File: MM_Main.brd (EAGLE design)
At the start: 72 x 92 mm, 76 parts, among them IC1 ULN2003AD, IC2 TB6612FNG, IC4 LD117ADT50TR, Q1 TEFT4300, Q2 TEFT4300, Q3 TEFT4300, Q4 TEFT4300, Q5 TEFT4300, Q6 TEFT4300, Q7 8MHz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

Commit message: wszystkie sciezki polaczone \!
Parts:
- removed C_V3: 100n, rcl:C0805
- removed R14, R15: 47k, resistor:R0805
- removed SG2: F/QMX, buzzer:F/QMX
- added BAT1, BOOT: (no value), pinhead:1X03
- added BUZ1: BUZZER-9.5MM-3V?, _microMouse:BUZZER-9.5MM
- added S2: (no value), adafruit:EG1218
- moved C21 80.5 mm to (18.4, -20.8), flipped to the bottom
- moved C22 71.9 mm to (11.7, -40.8), flipped to the bottom, turned to 90 degrees
- moved C_V2 70.0 mm to (7.14, 11.3)
- moved C_V1 63.1 mm to (7.94, -8.26), flipped to the bottom
- moved C15 56.8 mm to (11.6, -46.5), flipped to the bottom, turned to 270 degrees
- moved C11 45.3 mm to (6.99, -45.6), flipped to the bottom, turned to 270 degrees
- moved C13 44.5 mm to (-9.21, -29.8), flipped to the bottom
- moved IC4 37.6 mm to (17.2, -25.7), turned to 90 degrees
- moved BTN1 36.4 mm to (-23.7, -9.21)
- moved R11 35.9 mm to (-21.0, -4.76), flipped to the bottom, turned to 0 degrees
- moved RST_BTN 34.8 mm to (23.7, -4.45)
- moved BAT 28.0 mm to (22.8, -42.7), turned to 90 degrees
- moved FUSE1 24.6 mm to (18.4, -44.5)
- moved FUSE 24.4 mm to (18.4, -41.3)
- moved R12 17.2 mm to (-7.46, -52.9)
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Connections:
- removed net N$31: R14.1
- removed net N$33: R15.2
- removed net VDD1: C_V1.1
- removed net VDD2: C_V2.1
- removed net VDD3: C_V3.1
- removed net VSS1: C_V1.2
- removed net VSS2: C_V2.2
- removed net VSS3: C_V3.2
- net +3V3: now also C_V1.1, C_V2.1
- net +5V: now also BT-PROG.1, BT-PROG.2, BUZ1.+, C1.1, C6.+, IC1.9, R22.2, R25.1, R5.2, R6.2, R7.2, R8.2
- net +7V: no longer C1.1, C6.+, IC1.9, R22.2, R25.1, R5.2, R6.2, R7.2, R8.2, SG2.+
- net GND: now also C_V1.2, C_V2.2; no longer R14.2, R15.1
- net N$22: now also BUZ1.-; no longer SG2.-
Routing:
- net +7V: track 213.4 -> 78.2 mm, vias 6 -> 3
- net +5V: track 89.4 -> 219.8 mm, vias 2 -> 8
- net GNDA: track 85.3 -> 159.6 mm, vias 1 -> 2
- net GND: track 322.0 -> 375.1 mm
- net +3V3: track 344.6 -> 390.0 mm, vias 4 -> 6
- net RST: track 58.3 -> 32.2 mm
- net N$25: track 40.9 -> 33.1 mm
- net N$29: track 0.00 -> 5.17 mm, vias 0 -> 1
- net N$17: track 0.00 -> 5.15 mm, vias 0 -> 1
- net N$22: track 8.33 -> 11.5 mm
- net BTN: track 25.8 -> 28.9 mm, vias 2 -> 1
- net MR_PWM: track 57.3 -> 58.9 mm
- net BUZZER: track 17.0 -> 15.5 mm
- net N$1: track 2.13 -> 3.45 mm
- net ENCR_B: track 20.6 -> 21.5 mm
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- added copper zone on layer 16, net +5V
- added copper zone on layer 16, net TAJEMNICZY
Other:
- outline, holes or cut-outs redrawn
- board text added: "+3V3"
- board text added: "+5V"
- board text added: "GND"
- board text added: "RXD"
- board text added: "SWCLK"
- board text added: "SWDIO"
- board text added: "TXD"

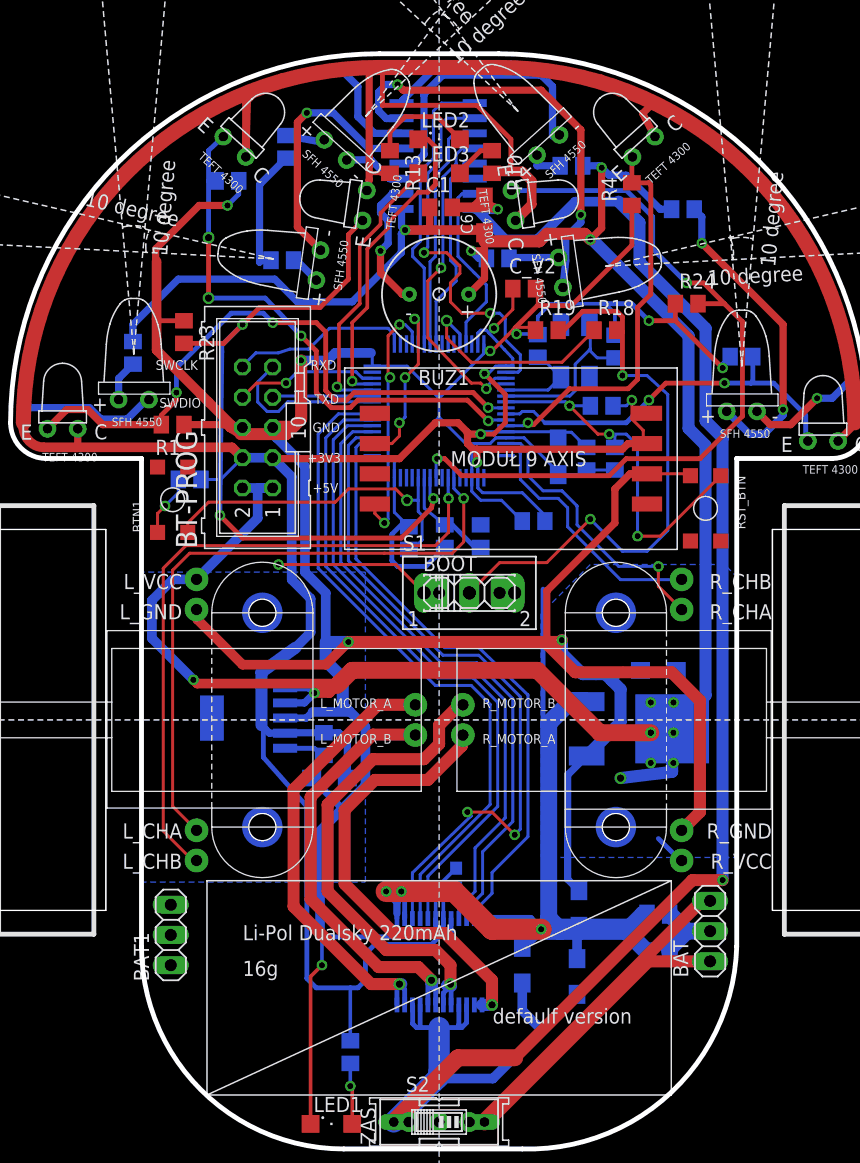
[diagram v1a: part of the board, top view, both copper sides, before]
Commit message: czesciowy DRC
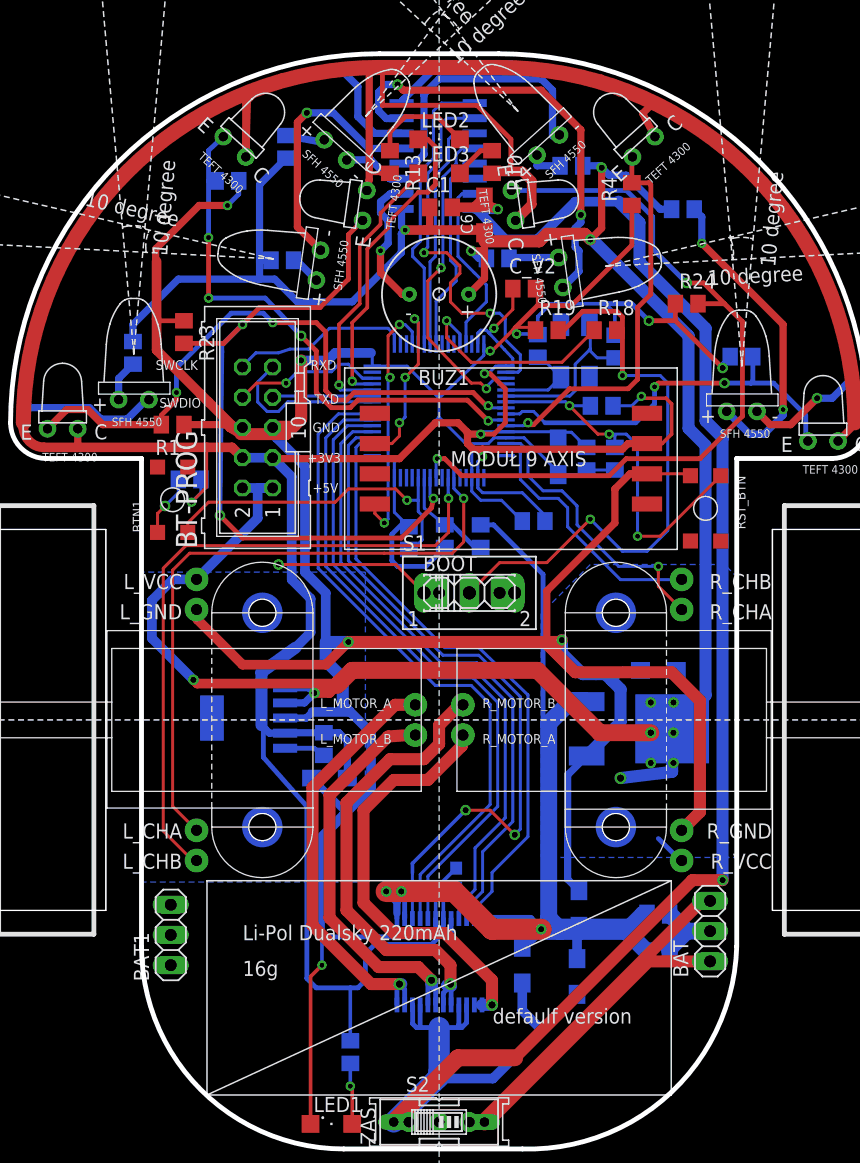
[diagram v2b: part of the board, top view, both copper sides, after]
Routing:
- net +7V: track 78.2 -> 86.4 mm
- net +3V3: track 390.0 -> 398.1 mm, vias 6 -> 7
- net +5V: track 219.8 -> 222.8 mm
- net N$9: track 38.5 -> 36.3 mm
- net N$19: track 37.3 -> 35.0 mm
- net N$20: track 38.5 -> 36.4 mm
- net N$18: track 41.4 -> 39.2 mm
- net GND: track 375.1 -> 376.3 mm
- net ADC_L: track 32.7 -> 33.5 mm
- net N$23: track 48.6 -> 49.3 mm
- net SWDIO: track 12.0 -> 12.5 mm

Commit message: renament - 4 LED + all on top
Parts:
- removed BT-PROG: (no value), con-ml:ML10
- removed C14: 100n, rcl:C0805
- removed C16: tant-a-4,7u, rcl:SMC_A
- removed D5, D6: SFH4545, _microMouse:SFH4545
- removed Q5, Q6: TEFT4300, _MM:TEFT4300
- removed R22, R23, R24, R25: (no value), rcl:R0805
- removed S2: (no value), adafruit:EG1218
- added C_VSSA: 100n, rcl:C0805
- added C_VSSA2: tant-a-4,7u, rcl:SMC_A
- added JP1: (no value), pinhead:2X04
- D1, D2, D3, D4: value SFH4545 -> SFH4545-C; device _microMouse:SFH4545 -> _microMouse:SFH4545-C
- moved FUSE1 727.3 mm to (-247.7, 632.5), flipped to the top, turned to 0 degrees
- moved FUSE 726.7 mm to (-254.0, 632.5), flipped to the top, turned to 0 degrees
- moved R9 721.2 mm to (-325.1, 632.5), flipped to the top, turned to 0 degrees
- moved C22 717.8 mm to (-233.7, 633.7), flipped to the top, turned to 0 degrees
- moved C12 714.1 mm to (-240.0, 633.7), flipped to the top, turned to 0 degrees
- moved C15 709.3 mm to (-189.2, 633.7), flipped to the top, turned to 0 degrees
- moved C11 704.6 mm to (-180.3, 633.7), flipped to the top, turned to 0 degrees
- moved R2 701.6 mm to (-289.6, 632.5), flipped to the top, turned to 0 degrees
- moved R20 699.3 mm to (-279.4, 632.5), flipped to the top, turned to 0 degrees
- moved C13 697.7 mm to (-224.8, 633.7), flipped to the top
- moved R5 695.3 mm to (-304.8, 632.5), flipped to the top
- moved R12 693.7 mm to (-106.7, 633.7), flipped to the top, turned to 0 degrees
- moved R17 692.9 mm to (-260.4, 632.5), flipped to the top, turned to 0 degrees
- moved R7 692.4 mm to (-315.0, 632.5), flipped to the top, turned to 0 degrees
- moved C21 692.3 mm to (-207.0, 633.7), flipped to the top
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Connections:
- removed net ADC: Q5.E, R23.2, U1.26
- removed net ADC2: Q6.E, R24.2, U1.25
- removed net INT_G: U$1.P$1
- removed net N$20: IC2.11, IC2.12, U$5.L_MOTOR_A
- removed net N$22: BUZ1.-, IC1.10
- removed net N$25: BAT.1, BAT.3, ZAS.1
- removed net N$3: D5.-, IC1.15
- removed net SCK: U1.51
- new net INT_A: U$1.P$1, U1.57
- new net N$30: U1.41
- new net N$32: U1.47
- new net N$34: U1.50
- new net N$35: U1.54
- new net N$36: U1.61
- new net N$37: U1.62
- new net N$38: U1.34
- new net N$39: U1.33
- new net N$40: U1.24
- new net N$41: U1.25
- net +3V3: now also C_VSSA.1, C_VSSA2.+, JP1.7, JP1.8; no longer BT-PROG.3, BT-PROG.4, C14.1, C16.+, Q5.C, Q6.C
- net +5V: no longer BT-PROG.1, BT-PROG.2, R22.2, R25.1
- net BTN: now also U1.26; no longer U1.28
- net BT_RXD: now also JP1.1; no longer BT-PROG.9
- net BT_TXD: now also JP1.3; no longer BT-PROG.7
- net BUZZER: now also U1.21; no longer U1.61
- net CS_A: now also U1.56
- net CS_G: now also U1.55
- net D_L: now also U1.16; no longer U1.55
- net D_LF: now also U1.15; no longer U1.54
- net D_LL: no longer IC1.2
- net D_R: now also U1.17; no longer U1.56
- net D_RF: now also IC1.6, U1.20; no longer U1.57
- net D_RR: no longer IC1.4
- net ENCR_A: now also U1.58; no longer U1.14
- net ENCR_B: now also U1.59; no longer U1.15
- net GND: now also C_VSSA.2, C_VSSA2.-, JP1.5, JP1.6; no longer BT-PROG.5, BT-PROG.6, C14.2, C16.-, R23.1, R24.1
- net GNDA: now also BAT.1, BAT.3; no longer ZAS.2
- net N$10: now also D2.ANODA; no longer D2.+
- net N$11: now also D3.ANODA; no longer D3.+
- net N$12: now also D4.ANODA; no longer D4.+
- net N$13: now also D1.KATODA; no longer D1.-
- net N$14: now also D2.KATODA; no longer D2.-
- net N$15: now also D3.KATODA, IC1.10; no longer D3.-, IC1.12
- net N$16: now also D4.KATODA; no longer D4.-
- net N$18: now also U$5.L_MOTOR_B; no longer U$5.R_MOTOR_B
- net N$19: now also BUZ1.-, IC1.12; no longer IC2.7, IC2.8, U$5.L_MOTOR_B
- net N$24: now also ZAS.2; no longer BAT.2
- net N$4: now also D1.ANODA; no longer D1.+
- net N$5: now also IC2.7, IC2.8, U$5.R_MOTOR_B; no longer D5.+, R22.1
- net N$6: now also IC2.11, IC2.12, U$5.R_MOTOR_A; no longer D6.-, IC1.13
- net N$7: now also IC2.1, IC2.2, U$5.L_MOTOR_A; no longer D6.+, R25.2
- net N$9: now also BAT.2, ZAS.1; no longer IC2.1, IC2.2, U$5.R_MOTOR_A
- net SCLK: now also U1.51
- net SWCLK: now also JP1.2; no longer BT-PROG.10
- net SWDIO: now also JP1.4; no longer BT-PROG.8
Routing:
- net GND: track 376.3 -> 47.0 mm, vias 9 -> 0
- net +3V3: track 398.1 -> 108.2 mm, vias 7 -> 4
- net GNDA: track 159.6 -> 13.9 mm, vias 2 -> 0
- net +5V: track 222.8 -> 95.9 mm, vias 8 -> 2
- net +7V: track 86.4 -> 0.00 mm, vias 3 -> 0
- net ADC2: track 65.7 -> 0.00 mm, vias 2 -> 0
- net ADC: track 60.7 -> 0.00 mm, vias 3 -> 0
- net N$13: track 59.4 -> 3.50 mm, vias 1 -> 0
- net N$23: track 49.3 -> 0.00 mm, vias 2 -> 0
- net SCLK: track 0.00 -> 44.0 mm
- net MR_IN2: track 56.1 -> 12.3 mm
- net MR_IN1: track 55.1 -> 12.2 mm
- net MR_PWM: track 58.9 -> 17.2 mm
- net ML_IN2: track 53.4 -> 13.2 mm
- net ML_IN1: track 52.3 -> 13.2 mm
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- removed copper zone on layer 16, net +5V
- removed copper zone on layer 16, net TAJEMNICZY
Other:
- board size 72 x 92 mm -> 101.4 x 83.6 mm
- board text added: "0"
- board text added: "10"
- board text added: "20"
- board text added: "30"
- board text added: "40"
- board text added: "50"
- board text removed: "+3V3"
- board text removed: "+5V"
- board text removed: "GND"
- board text removed: "RXD"
- board text removed: "SWCLK"
- board text removed: "SWDIO"
- board text removed: "TXD"

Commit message: rozwoj brd
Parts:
- moved R9 775.2 mm to (-240.8, -138.1), turned to 90 degrees
- moved R20 725.9 mm to (-240.8, -92.4), turned to 90 degrees
- moved R17 706.1 mm to (-240.8, -73.3), turned to 90 degrees
- moved R6 701.6 mm to (25.2, 16.0), turned to 270 degrees
- moved FUSE 692.1 mm to (-30.3, -22.5), turned to 90 degrees
- moved R1 690.9 mm to (27.6, 16.0), turned to 90 degrees
- moved R8 690.9 mm to (9.21, 25.1)
- moved FUSE1 689.4 mm to (-32.5, -22.5), turned to 90 degrees
- moved C12 686.8 mm to (-242.1, -53.0), turned to 90 degrees
- moved R13 681.8 mm to (17.8, -35.4), turned to 180 degrees
- moved C22 680.5 mm to (-242.1, -46.7), turned to 90 degrees
- moved R7 680.1 mm to (-10.2, 24.4), turned to 270 degrees
- moved R5 677.1 mm to (-25.2, 15.7), turned to 270 degrees
- moved R10 677.1 mm to (17.8, -33.0), turned to 180 degrees
- moved LED3 676.5 mm to (27.5, -24.0), turned to 270 degrees
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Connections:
- removed net N$36: U1.61
- removed net N$37: U1.62
- new net N$42: U1.30
- net LED1: now also U1.62; no longer U1.45
- net LED2: now also U1.61; no longer U1.44
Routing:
- net +7V: track 0.00 -> 79.8 mm, vias 0 -> 2
- net GNDA: track 13.9 -> 87.1 mm, vias 0 -> 4
- net +3V3: track 108.2 -> 165.6 mm, vias 4 -> 5
- net LED1: track 0.00 -> 55.8 mm
- net LED2: track 0.00 -> 53.9 mm
- net GND: track 47.0 -> 75.4 mm
- net N$21: track 0.00 -> 16.9 mm
- net N$8: track 0.00 -> 13.7 mm
- net MISO: track 45.0 -> 33.2 mm, vias 0 -> 2
- net N$19: track 45.1 -> 53.3 mm
- net N$24: track 0.00 -> 7.33 mm
- net N$9: track 0.00 -> 7.11 mm
- net ADC_RF: track 27.3 -> 34.4 mm
- net MOSI: track 36.4 -> 29.4 mm
- net SCLK: track 44.0 -> 37.0 mm
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
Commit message: aktualizacja brd
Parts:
- moved R21 294.2 mm to (16.5, 2.22), turned to 180 degrees
- moved C_OSC1 279.0 mm to (12.5, 19.5)
- moved C2 277.8 mm to (16.7, -1.59), turned to 180 degrees
- moved C_OSC2 276.8 mm to (12.5, 16.2), turned to 0 degrees
- moved R9 264.4 mm to (-7.30, -14.1), turned to 0 degrees
- moved R17 243.1 mm to (-6.19, -9.84), turned to 270 degrees
- moved C22 223.5 mm to (-19.4, -28.6)
- moved R20 221.6 mm to (-35.7, -8.57), turned to 270 degrees
- moved R11 221.2 mm to (-32.7, -8.89)
- moved C6 219.8 mm to (-26.0, 11.6), turned to 0 degrees
- moved C21 188.6 mm to (-53.8, -30.3)
- moved C1 86.7 mm to (-26.4, 9.68)
- moved BAT1 18.2 mm to (-22.7, -17.5), turned to 270 degrees
- moved R18 14.6 mm to (15.2, 25.2)
- moved BAT 3.65 mm to (-22.9, -26.0)
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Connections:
- net GNDA: now also BAT1.1, BAT1.3
- net N$9: now also BAT1.2
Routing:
- net GND: track 75.4 -> 285.2 mm, vias 0 -> 6
- net +3V3: track 165.6 -> 282.2 mm, vias 5 -> 8
- net +5V: track 94.9 -> 166.3 mm, vias 3 -> 7
- net N$16: track 30.1 -> 49.6 mm
- net OSC_OUT: track 5.17 -> 24.6 mm, vias 0 -> 2
- net N$23: track 0.00 -> 18.6 mm, vias 0 -> 1
- net BOOT0: track 9.98 -> 27.8 mm, vias 0 -> 2
- net RST: track 58.4 -> 72.9 mm, vias 0 -> 2
- net ADC_VBAT: track 31.9 -> 45.8 mm
- net OSC_IN: track 3.91 -> 15.9 mm, vias 0 -> 2
- net GNDA: track 87.1 -> 98.7 mm
- net ADC_RF: track 34.4 -> 44.9 mm, vias 1 -> 2
- net ADC_L: track 12.0 -> 22.4 mm
- net N$19: track 53.3 -> 63.2 mm
- net N$9: track 7.11 -> 15.1 mm
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
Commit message: brd prawie gotowe
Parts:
- C15: value tant-a-100u -> tant-d-220u; device rcl:SMC_A -> rcl:SMC_D
- moved BOOT 241.9 mm to (0.95, 25.7), turned to 180 degrees
- moved C13 238.0 mm to (-8.89, 9.53), turned to 270 degrees
- moved C12 237.7 mm to (-8.73, -7.94), turned to 270 degrees
- moved C15 224.7 mm to (-18.7, -26.8)
- moved C11 130.1 mm to (-113.8, -14.9)
- moved C21 39.4 mm to (-23.3, -5.40), turned to 180 degrees
- moved R20 17.6 mm to (-23.3, 3.97)
- moved R11 12.2 mm to (-23.3, -1.11), turned to 270 degrees
- moved C22 4.46 mm to (-14.9, -28.9)
- moved IC4 2.13 mm to (-12.7, -20.2)
- moved BAT1 0.48 mm to (-22.7, -17.9)
- moved BTN1 0.32 mm to (-35.6, -17.1)
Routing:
- net +3V3: track 282.2 -> 344.8 mm, vias 8 -> 10
- net GND: track 285.2 -> 333.6 mm, vias 6 -> 7
- net +5V: track 166.3 -> 197.1 mm, vias 7 -> 13
- net BTN: track 52.9 -> 78.9 mm, vias 0 -> 3
- net N$29: track 0.00 -> 24.4 mm, vias 0 -> 2
- net GNDA: track 98.7 -> 113.0 mm
- net +7V: track 81.6 -> 87.6 mm
- net RST: track 72.9 -> 77.7 mm
- net N$1: track 0.00 -> 2.38 mm
- net ADC_VBAT: track 45.8 -> 46.9 mm, vias 0 -> 2

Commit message: wszystko polaczone, trzeba dopiscic
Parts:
- added R14: pcb, resistor:R0201
- moved L1 148.4 mm to (136.7, 57.6), turned to 45 degrees
- moved R13 9.58 mm to (9.21, -31.1)
- moved R10 4.69 mm to (13.5, -31.1), turned to 0 degrees
- moved Q1 1.43 mm to (31.3, 18.9), turned to 353 degrees
- moved Q4 0.95 mm to (-31.1, 18.7), turned to 7 degrees
- moved R12 0.35 mm to (17.9, -31.1)
- moved RST_BTN 0.32 mm to (29.8, -17.6)
- turned D1 to 7 degrees
- turned D2 to 353 degrees
- turned D3 to 36 degrees
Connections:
- net GND: now also R14.1
- net GNDA: now also R14.2
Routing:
- net CS_A: track 31.9 -> 46.5 mm
- net INT_A: track 23.6 -> 37.9 mm
- net CS_G: track 31.9 -> 46.2 mm
- net MOSI: track 29.4 -> 43.3 mm
- net BT_TXD: track 32.4 -> 44.7 mm
- net MISO: track 33.2 -> 45.6 mm
- net SWDIO: track 34.7 -> 46.5 mm
- net SWCLK: track 43.3 -> 54.8 mm
- net N$21: track 16.9 -> 24.2 mm
- net N$8: track 13.7 -> 20.3 mm
- net +3V3: track 344.8 -> 349.5 mm
- net SCLK: track 37.0 -> 38.9 mm
- net GNDA: track 113.0 -> 114.8 mm
- net GND: track 333.6 -> 335.4 mm
- net ADC_LF: track 42.6 -> 41.5 mm
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- added copper zone on layer 1, net +5V
- added copper zone on layer 16, net +5V
